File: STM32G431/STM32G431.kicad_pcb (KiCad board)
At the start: 4 copper layers, 60 x 44 mm, 153 parts, among them J1 W, J10 NTC, J11 LED, J2 U, J3 V, J4 GND, J5 VIN, J6 UART, J8 HALL, J9 AIN/PWM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

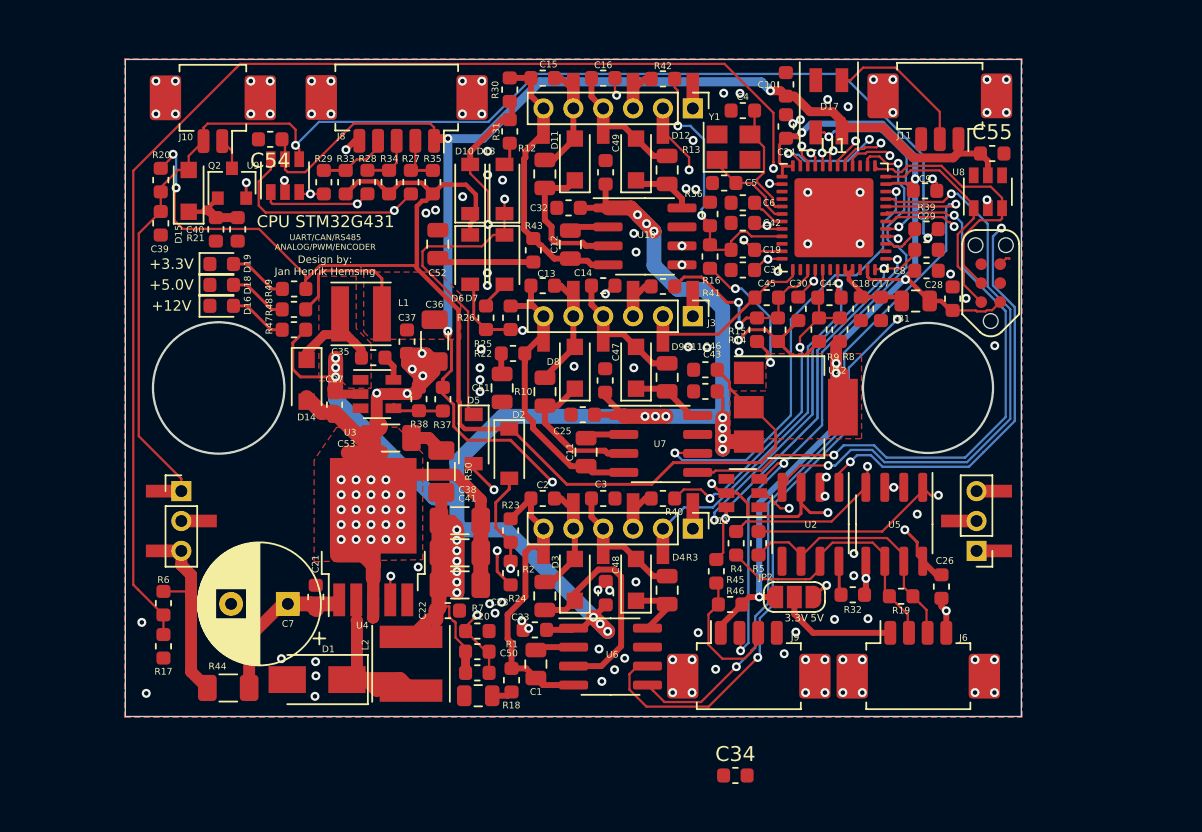
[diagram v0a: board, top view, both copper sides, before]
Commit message: updated layout
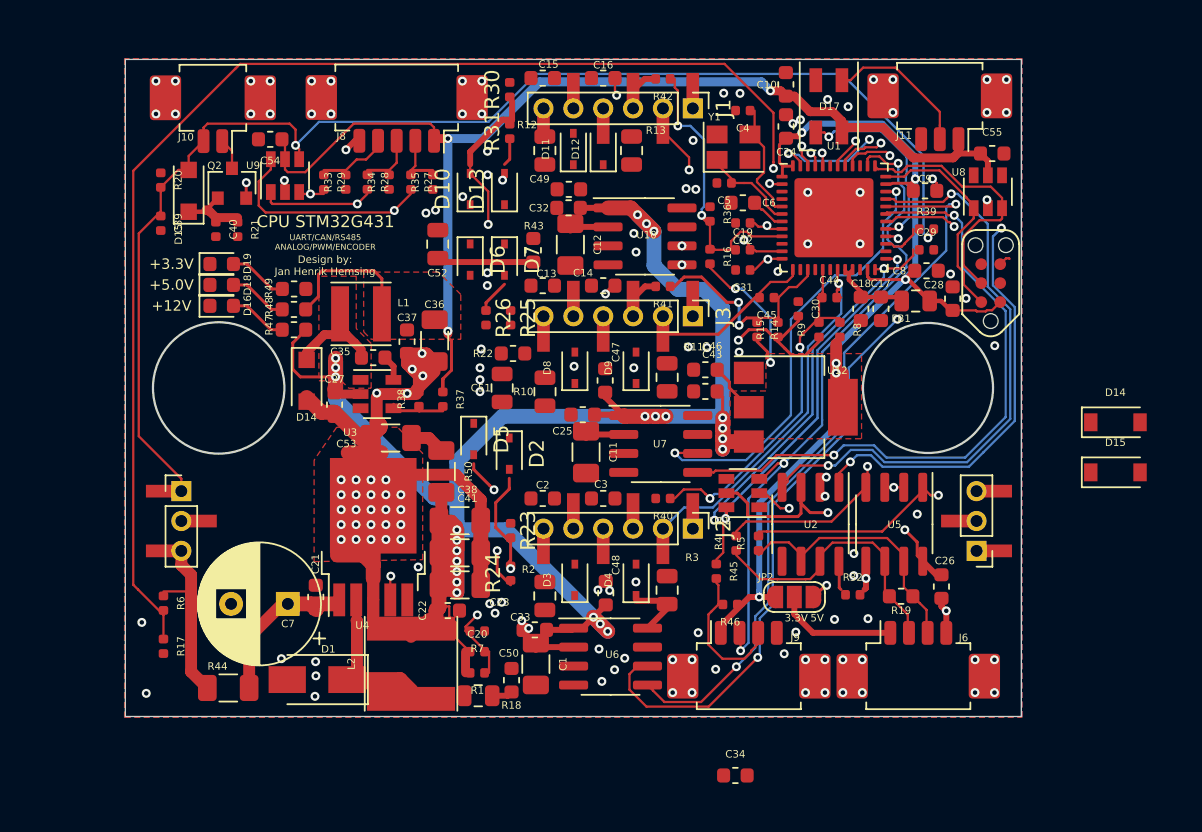
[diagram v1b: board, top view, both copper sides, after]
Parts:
- added D14: B5819W, Diode_SMD:D_SOD-123, F.Cu at (86.3, 47.3)
- added D15: B5819W, Diode_SMD:D_SOD-123, F.Cu at (86.3, 50.6)
- C1, C11, C12: footprint Capacitor_SMD:C_0805_2012Metric -> Capacitor_SMD:C_1206_3216Metric
- C19: value 100p -> DNP; footprint Capacitor_SMD:C_0603_1608Metric -> Capacitor_SMD:C_0402_1005Metric
- C20, C29, C30, C31, C4, C42, C44, C45, C5: footprint Capacitor_SMD:C_0603_1608Metric -> Capacitor_SMD:C_0402_1005Metric
- C39, C40: footprint Capacitor_SMD:C_0603_1608Metric -> Resistor_SMD:R_0402_1005Metric
- D10, D13, D2, D5, D6, D7: value B5819W -> 1N5819WS; footprint Diode_SMD:D_SOD-123 -> Diode_SMD:D_SOD-323
- D11, D12, D3, D4, D8, D9: value SM4007PL -> B16WS; footprint Diode_SMD:D_SOD-123F -> Diode_SMD:D_SOD-323
- L2: footprint Inductor_SMD:L_Taiyo-Yuden_MD-5050 -> Inductor_SMD:L_Taiyo-Yuden_NR-60xx
- R1, R20, R21, R23, R24, R25, R26, R27, R28, R29, R30, R31, R32, R33, R34, R35, R37, R38, R39, R4, R45, R46, R5, R7: footprint Resistor_SMD:R_0603_1608Metric -> Resistor_SMD:R_0402_1005Metric
- R14, R15, R16, R17, R36, R40, R41, R42, R6, R8, R9: footprint Resistor_SMD:R_0603_1608Metric -> Capacitor_SMD:C_0402_1005Metric
- moved R13 2.71 mm to (53.9, 29.1)
- moved C49 2.71 mm to (49.7, 31.7), turned to 180 degrees
- moved D12 2.31 mm to (52.0, 29.0)
- moved R12 1.57 mm to (48.1, 29.1)
- moved D11 0.71 mm to (50.0, 29.0)
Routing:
- net +3V3: track 170.2 -> 87.4 mm, vias 10 -> 8
- net GPIO_BEMF: track 46.2 -> 0.00 mm, vias 2 -> 0
- net UV: track 29.8 -> 0.00 mm, vias 2 -> 0
- net +5V: track 134.7 -> 112.4 mm, vias 8 -> 6
- net U: track 19.9 -> 0.00 mm
- net V: track 19.5 -> 0.00 mm
- net W: track 18.9 -> 0.00 mm
- net Net-(D3-Pad1): track 15.1 -> 0.00 mm
- net Net-(D11-Pad1): track 9.86 -> 0.00 mm
- net Net-(D8-Pad1): track 9.75 -> 0.00 mm
- net Net-(C14-Pad1): track 8.66 -> 0.00 mm
- net Net-(C16-Pad1): track 8.66 -> 0.00 mm
- net Net-(C3-Pad1): track 8.65 -> 0.00 mm
- net Net-(C13-Pad2): track 7.80 -> 0.00 mm
- net Net-(C2-Pad2): track 7.52 -> 0.00 mm
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
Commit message: updated layout
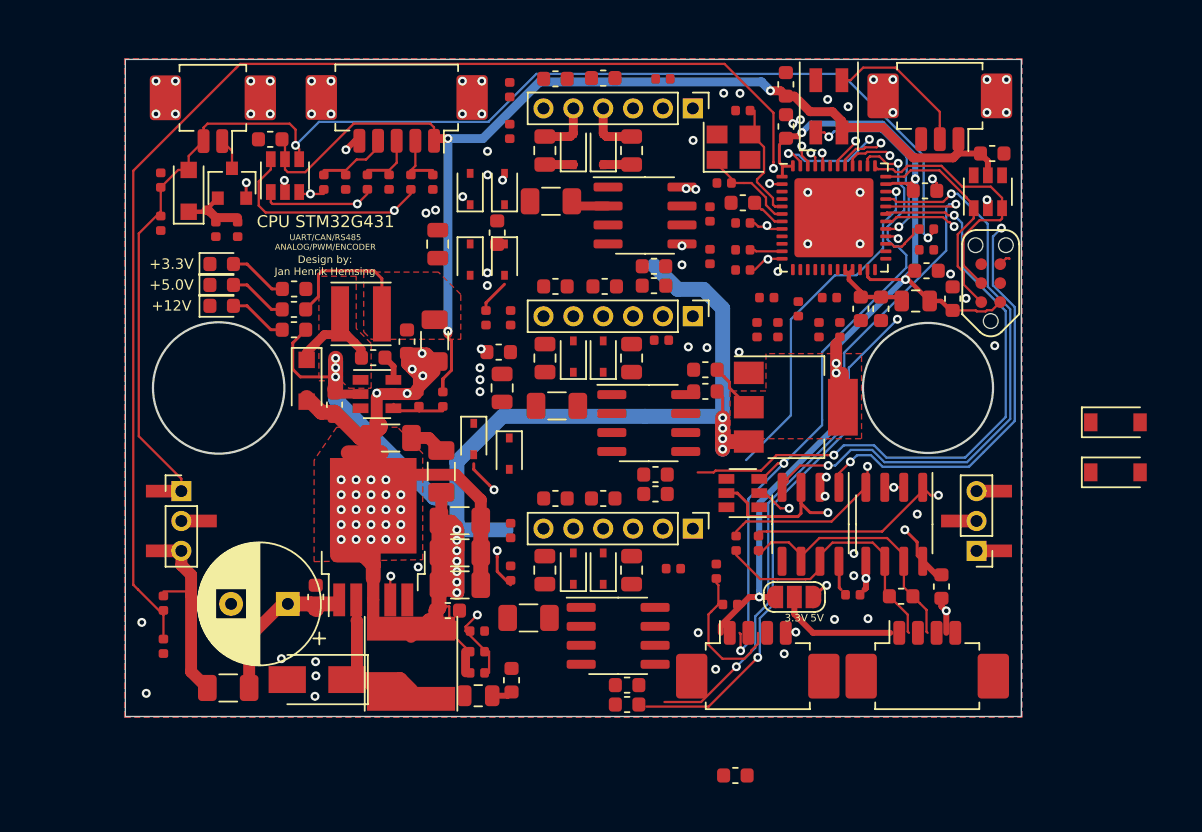
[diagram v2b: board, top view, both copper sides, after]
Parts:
- J1, J2, J3: footprint otter:PinHeader_1x06_P2.00mm_Vertical_COMBI -> otter:PinHeader_1x06_P2.00mm_Vertical
- moved C49 8.61 mm to (55.4, 38.1), turned to 0 degrees
- moved C47 8.31 mm to (55.5, 52.1), turned to 0 degrees
- moved C48 7.60 mm to (53.6, 66.2), turned to 0 degrees
- moved C33 7.20 mm to (53.6, 64.9), turned to 0 degrees
- moved C32 6.93 mm to (55.4, 36.9), turned to 0 degrees
- moved C25 6.31 mm to (55.5, 50.8), turned to 0 degrees
- moved R40 4.75 mm to (56.7, 57.1)
- moved C11 3.66 mm to (48.9, 46.2), turned to 180 degrees
- moved R41 3.60 mm to (55.9, 41.8)
- moved C12 3.18 mm to (48.5, 32.5), turned to 180 degrees
- moved C1 3.13 mm to (47.0, 60.4), turned to 180 degrees
- moved R3 2.73 mm to (53.9, 57.2)
- moved R11 2.71 mm to (53.9, 43.0)
- moved R43 2.69 mm to (44.9, 34.6)
- moved D4 2.32 mm to (52.0, 57.1)
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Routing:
- net UU: track 47.9 -> 0.00 mm, vias 3 -> 0
- net +12V: track 146.0 -> 113.8 mm, vias 23 -> 14
- net Ain: track 27.5 -> 0.00 mm, vias 2 -> 0
- net IUL: track 26.4 -> 0.00 mm, vias 1 -> 0
- net IUH: track 23.1 -> 0.00 mm, vias 2 -> 0
- net IWH: track 19.5 -> 0.00 mm, vias 2 -> 0
- net UW: track 32.9 -> 18.0 mm, vias 2 -> 1
- net IVH: track 14.0 -> 0.00 mm, vias 2 -> 0
- net IWL: track 14.0 -> 1.90 mm, vias 2 -> 0
- net IVL: track 12.0 -> 0.00 mm
- net GND: track 79.6 -> 68.8 mm, vias 145 -> 107
- net +3V3: track 87.4 -> 77.5 mm, vias 8 -> 6
- net VL: track 30.2 -> 23.7 mm, vias 2 -> 1
- net Net-(C52-Pad2): track 6.51 -> 0.00 mm
- net Net-(D4-Pad1): track 4.33 -> 0.00 mm
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
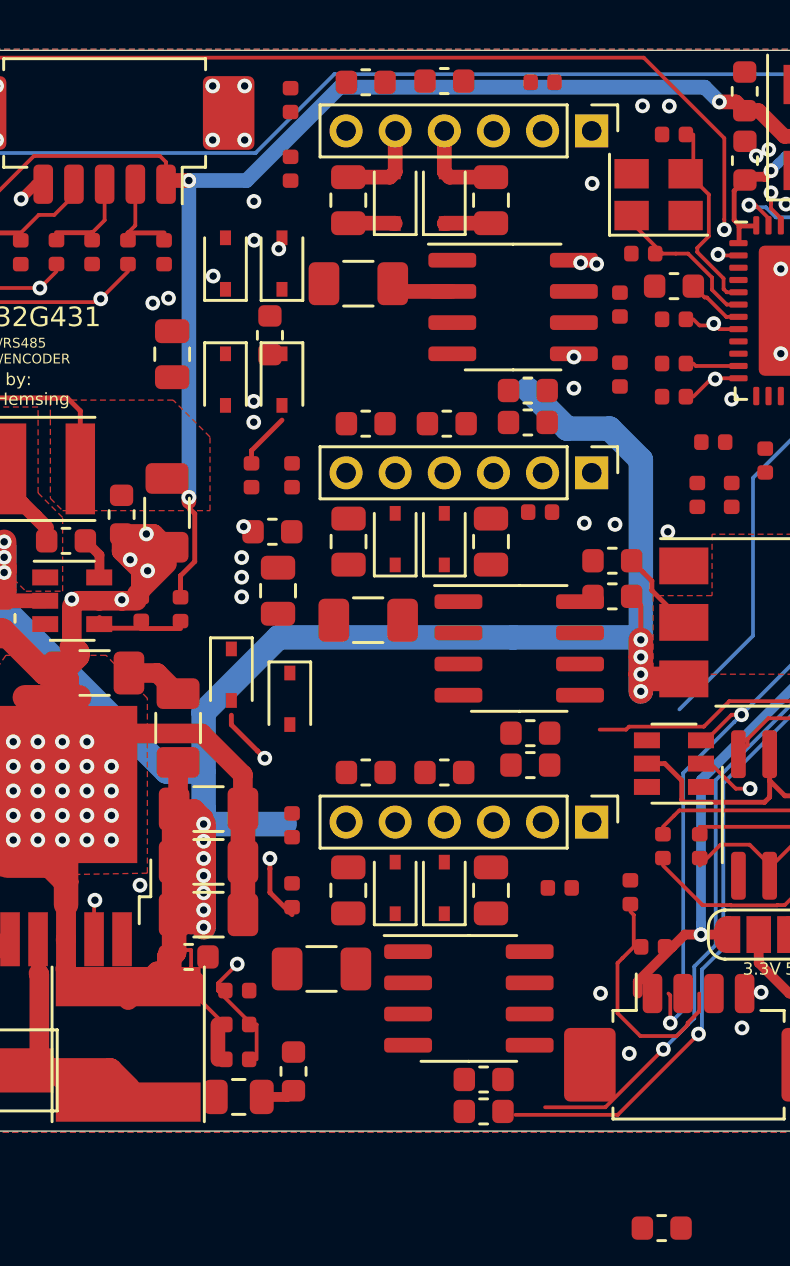
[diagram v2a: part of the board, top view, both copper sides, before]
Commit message: updated layout
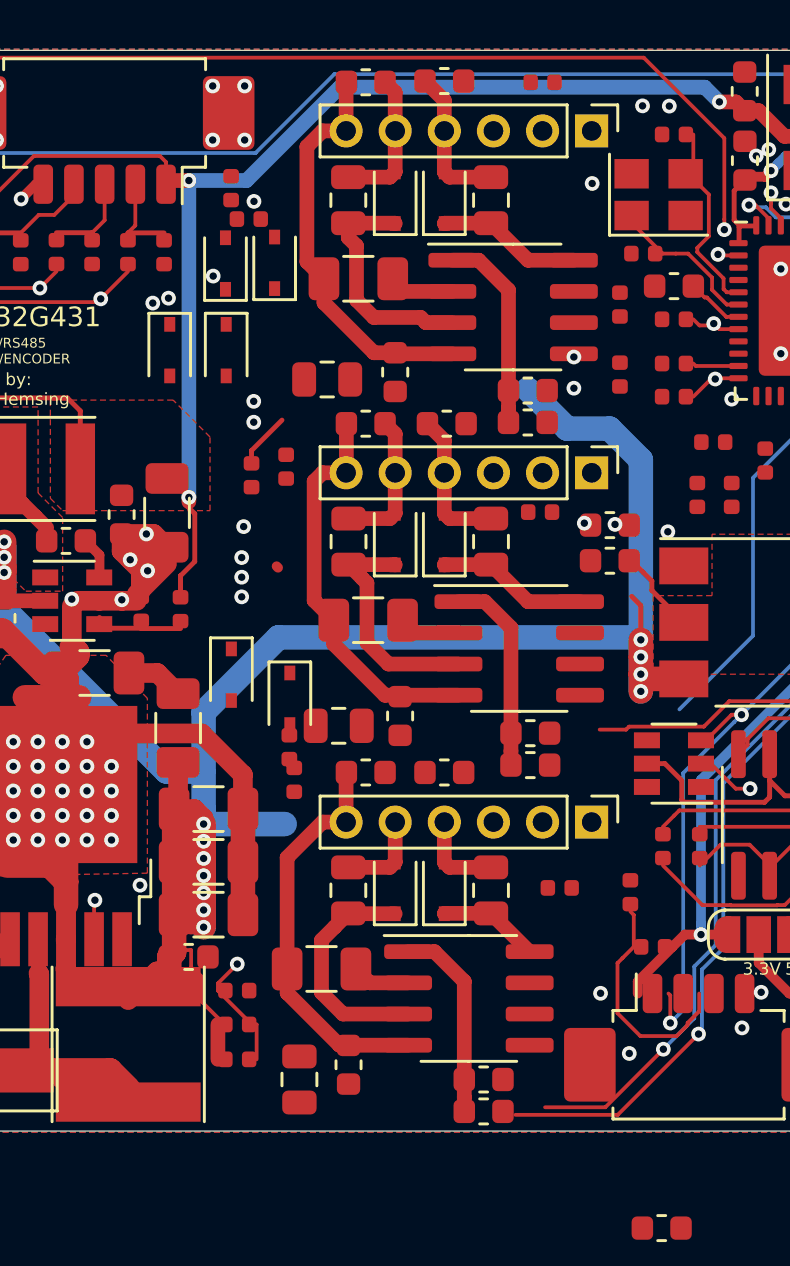
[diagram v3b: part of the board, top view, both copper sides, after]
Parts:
- moved R22 9.13 mm to (50.2, 50.1), turned to 90 degrees
- moved C52 6.39 mm to (47.2, 36.4), turned to 0 degrees
- moved R24 6.03 mm to (45.7, 51.4)
- moved C51 6.03 mm to (47.7, 50.5), turned to 0 degrees
- moved R43 5.32 mm to (50.0, 36.1)
- moved R30 4.33 mm to (43.3, 28.6)
- moved R31 2.66 mm to (44.0, 29.9), turned to 180 degrees
- moved C50 2.57 mm to (46.1, 64.9), turned to 90 degrees
- moved D6 2.57 mm to (40.8, 35.2)
- moved D7 2.57 mm to (43.1, 35.2)
- moved R18 2.26 mm to (48.1, 64.3)
- moved R23 1.85 mm to (45.9, 52.7)
- moved C46 1.45 mm to (58.7, 42.3)
- moved C43 1.45 mm to (58.7, 43.8)
- moved R25 0.42 mm to (45.6, 40.0)
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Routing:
- net +12V: track 113.8 -> 138.2 mm
- net W: track 0.00 -> 16.6 mm
- net V: track 0.00 -> 16.3 mm
- net U: track 0.00 -> 16.3 mm
- net Net-(D3-Pad1): track 0.00 -> 9.48 mm
- net Net-(D8-Pad1): track 0.00 -> 9.48 mm
- net Net-(D5-Pad2): track 9.14 -> 0.00 mm, vias 2 -> 0
- net Net-(D11-Pad1): track 1.92 -> 9.46 mm
- net Net-(D9-Pad1): track 0.00 -> 6.15 mm
- net Net-(C14-Pad1): track 0.00 -> 5.92 mm
- net Net-(C13-Pad2): track 0.00 -> 5.81 mm
- net Net-(D4-Pad1): track 0.00 -> 4.13 mm
- net Net-(D12-Pad1): track 1.91 -> 5.90 mm, vias 2 -> 0
- net Net-(C2-Pad2): track 0.00 -> 3.63 mm
- net Net-(C3-Pad1): track 0.00 -> 3.62 mm
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
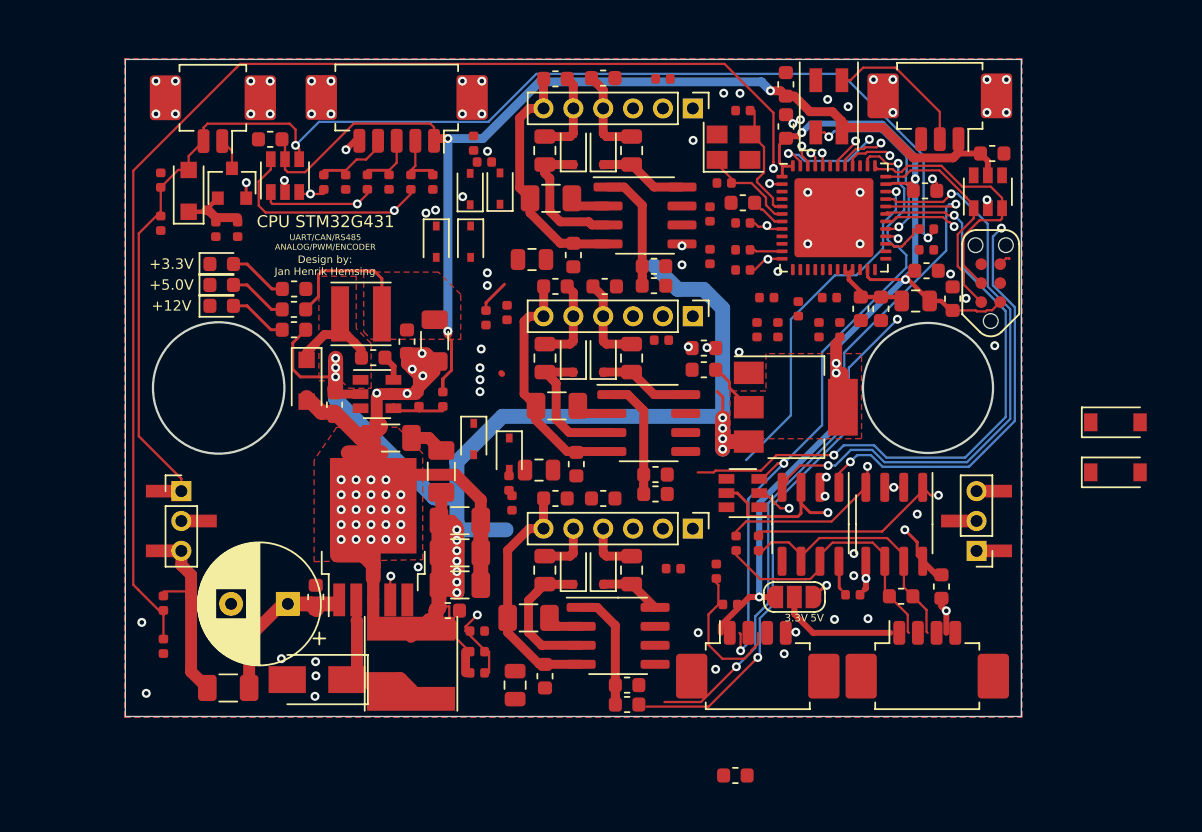
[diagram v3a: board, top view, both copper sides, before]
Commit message: updated layout
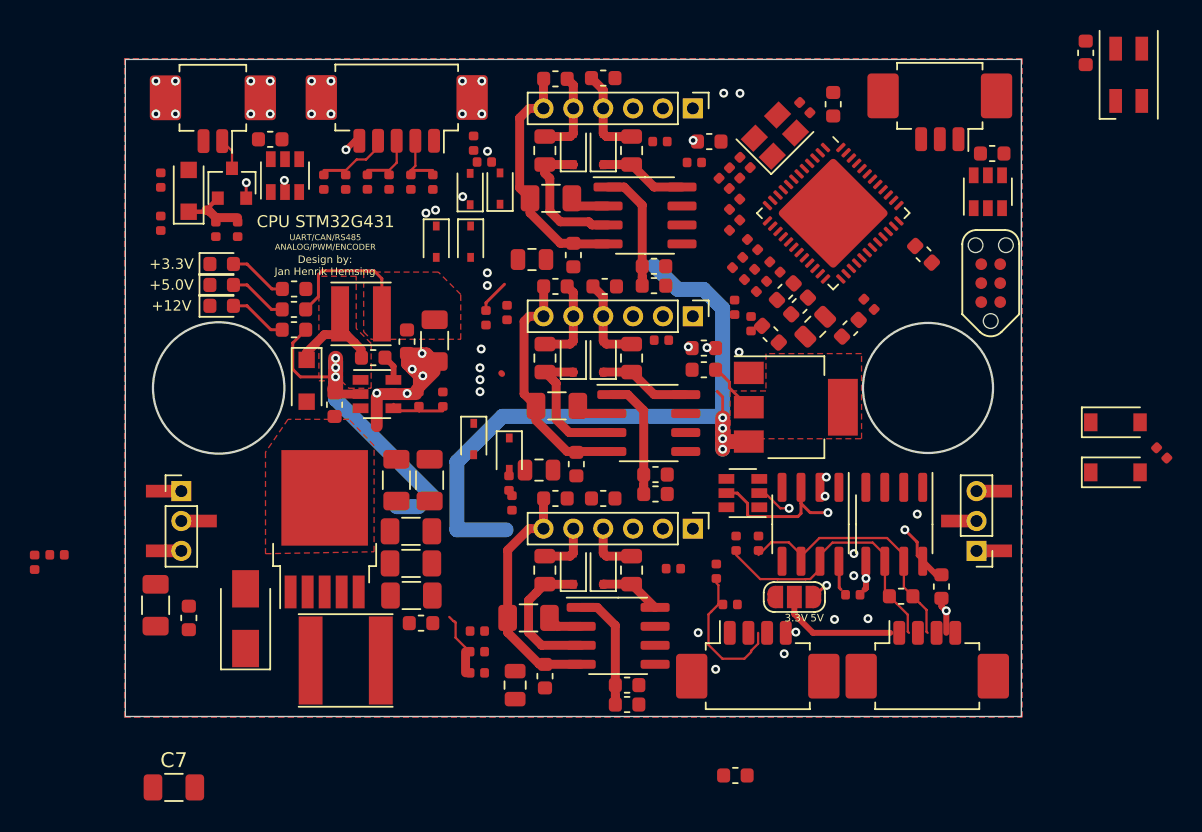
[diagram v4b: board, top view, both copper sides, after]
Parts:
- C7: value 100u 100V -> 10u; footprint Capacitor_THT:CP_Radial_D8.0mm_P3.80mm -> Capacitor_SMD:C_1206_3216Metric
- moved R39 21.7 mm to (89.4, 49.4), turned to 315 degrees
- moved C10 20.2 mm to (84.3, 22.6)
- moved D17 20.2 mm to (87.2, 24.0)
- moved C7 14.5 mm to (23.2, 71.8), turned to 0 degrees
- moved C28 12.4 mm to (63.2, 41.4), turned to 135 degrees
- moved R17 10.3 mm to (13.9, 56.7)
- moved C21 8.61 mm to (24.2, 60.4)
- moved R6 7.83 mm to (15.4, 56.2), turned to 180 degrees
- moved R44 7.37 mm to (22.0, 59.5), turned to 270 degrees
- moved FB1 6.94 mm to (66.2, 40.9), turned to 225 degrees
- moved C8 6.39 mm to (68.5, 41.0), turned to 225 degrees
- moved R16 6.39 mm to (58.1, 29.9), turned to 0 degrees
- moved D1 6.29 mm to (28.1, 60.5), turned to 90 degrees
- moved R8 5.96 mm to (61.9, 40.7)
- moved C17 5.45 mm to (65.1, 39.5), turned to 225 degrees
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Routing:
- net NTC_EXT: track 90.2 -> 0.00 mm, vias 2 -> 0
- net Vin_mon: track 89.6 -> 0.00 mm, vias 2 -> 0
- net +5V: track 112.4 -> 35.9 mm, vias 6 -> 3
- net +3V3: track 77.5 -> 3.64 mm, vias 6 -> 0
- net HALL1: track 53.3 -> 0.00 mm, vias 2 -> 0
- net UART_RX: track 49.9 -> 0.00 mm, vias 2 -> 0
- net UART_TX: track 49.1 -> 0.00 mm, vias 2 -> 0
- net CANTX: track 48.5 -> 0.00 mm, vias 4 -> 0
- net UH: track 48.1 -> 0.00 mm, vias 2 -> 0
- net HALL2: track 47.8 -> 0.00 mm, vias 2 -> 0
- net HALL3: track 44.8 -> 0.00 mm, vias 2 -> 0
- net PWM: track 44.7 -> 0.00 mm, vias 3 -> 0
- net UL: track 42.7 -> 0.00 mm, vias 3 -> 0
- net VH: track 42.6 -> 0.05 mm, vias 2 -> 0
- net CANRX: track 39.7 -> 0.00 mm, vias 2 -> 0
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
